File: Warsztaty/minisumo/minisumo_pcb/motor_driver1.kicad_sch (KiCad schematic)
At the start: 6 parts, among them U2 TB6612FNG

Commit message: stan przed usunięciem jednego czujnika lini
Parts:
- C3, C6: footprint Capacitor_SMD:C_0805_2012Metric_Pad1.18x1.45mm_HandSolder -> Capacitor_SMD:C_0805_2012Metric
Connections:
- net MOTOR_IN1: now reaches M1.2, U2.1 (AO1), U2.11 (BO1), U2.12 (BO1), U2.2 (AO1)
- net MOTOR_IN2: now reaches M1.1, U2.5 (AO2), U2.6 (AO2), U2.7 (BO2), U2.8 (BO2)
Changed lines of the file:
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@@
+		)
+	)
+	(label "MOTOR_IN1"
+		(at 76.2 45.72 0)
+		(fields_autoplaced yes)
+		(effects
+			(font
+				(size 1.27 1.27)
+			)
+			(justify left bottom)
+		)
+	)
+	(label "MOTOR_IN2"
+		(at 76.2 55.88 0)
+		(fields_autoplaced yes)
+		(effects
+			(font
+				(size 1.27 1.27)
+			)
+			(justify left bottom)
 		)
 	)
@@
 			)
 		)
-		(property "Footprint" "Capacitor_SMD:C_0805_2012Metric_Pad1.18x1.45mm_HandSolder"
+		(property "Footprint" "Capacitor_SMD:C_0805_2012Metric"
 			(at 31.75 30.48 0)
 			(effects
@@
 			)
 		)
-		(property "Footprint" "Capacitor_SMD:C_0805_2012Metric_Pad1.18x1.45mm_HandSolder"
+		(property "Footprint" "Capacitor_SMD:C_0805_2012Metric"
 			(at 72.39 29.21 0)
 			(effects

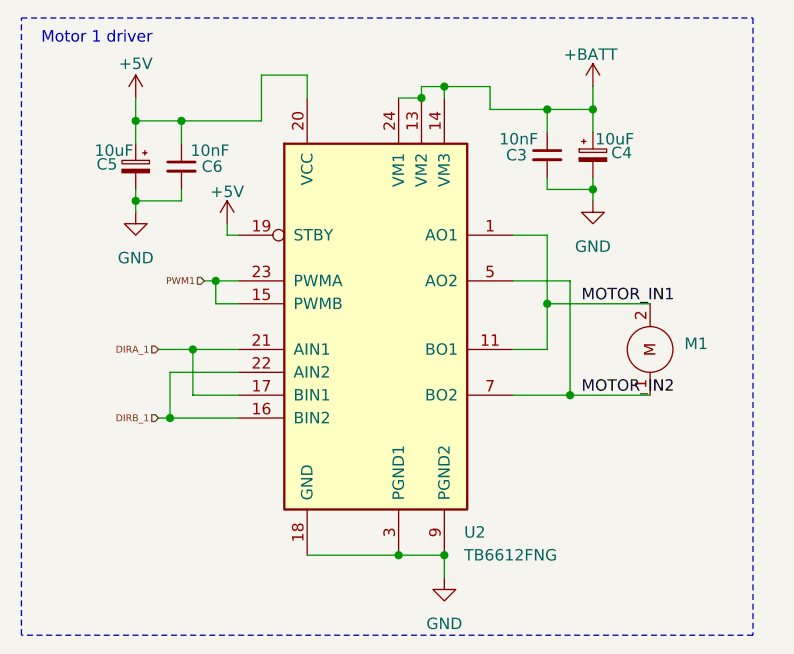
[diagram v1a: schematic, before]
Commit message: Wstępny wyglad robota i płytki
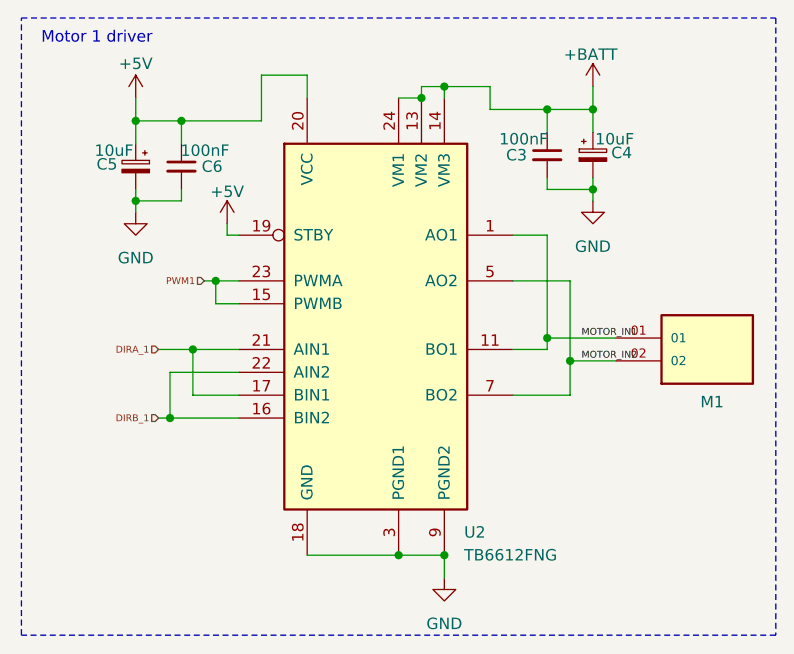
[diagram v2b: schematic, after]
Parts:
- removed M1: ~, Motors_KoNaR:KoNaR_Motor, symbol Motors_KoNaR:Motor
- added M1: HTSW-102-08-L-S, HTSW-102-08-L-S:SAMTEC_HTSW-102-08-L-S, symbol HTSW-102-08-L-S:HTSW-102-08-L-S
- C3, C6: value 10nF -> 100nF
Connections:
- net MOTOR_IN1: now also M1.01
- net MOTOR_IN2: now also M1.02
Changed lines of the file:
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@@
+	)
+	(junction
+		(at 74.93 52.07)
+		(diameter 0)
+		(color 0 0 0 0)
 	)
 	(junction
@@
 	)
 	(junction
-		(at 72.39 45.72)
+		(at 72.39 49.53)
 		(diameter 0)
 		(color 0 0 0 0)
@@
 	)
 	(junction
-		(at 74.93 55.88)
-		(diameter 0)
-		(color 0 0 0 0)
-	)
-	(junction
 		(at 30.48 58.42)
 		(diameter 0)
@@
 	(wire
 		(pts
-			(xy 72.39 38.1) (xy 72.39 45.72)
-		)
-		(stroke
-			(width 0)
-			(type default)
-		)
-	)
-	(wire
-		(pts
 			(xy 30.48 53.34) (xy 30.48 58.42)
 		)
@@
 	(wire
 		(pts
-			(xy 74.93 43.18) (xy 74.93 55.88)
+			(xy 74.93 43.18) (xy 74.93 52.07)
 		)
 		(stroke
@@
 	(wire
 		(pts
-			(xy 72.39 45.72) (xy 83.82 45.72)
-		)
-		(stroke
-			(width 0)
-			(type default)
-		)
-	)
-	(wire
-		(pts
 			(xy 45.72 73.66) (xy 55.88 73.66)
 		)
@@
 	(wire
 		(pts
+			(xy 72.39 49.53) (xy 80.01 49.53)
+		)
+		(stroke
+			(width 0)
+			(type default)
+		)
+	)
+	(wire
+		(pts
 			(xy 36.83 36.83) (xy 36.83 38.1)
 		)
@@
 	(wire
 		(pts
+			(xy 72.39 38.1) (xy 72.39 49.53)
+		)
+		(stroke
+			(width 0)
+			(type default)
+		)
+	)
+	(wire
+		(pts
+			(xy 74.93 52.07) (xy 80.01 52.07)
+		)
+		(stroke
+			(width 0)
+			(type default)
+		)
+	)
+	(wire
+		(pts
+			(xy 72.39 49.53) (xy 72.39 50.8)
+		)
+		(stroke
+			(width 0)
+			(type default)
+		)
+	)
+	(wire
+		(pts
+			(xy 74.93 52.07) (xy 74.93 55.88)
+		)
+		(stroke
+			(width 0)
+			(type default)
+		)
+	)
+	(wire
+		(pts
 			(xy 31.75 25.4) (xy 31.75 27.94)
 		)
@@
 	(wire
 		(pts
-			(xy 72.39 45.72) (xy 72.39 50.8)
-		)
-		(stroke
-			(width 0)
-			(type default)
-		)
-	)
-	(wire
-		(pts
 			(xy 45.72 20.32) (xy 45.72 22.86)
 		)
@@
 		(pts
 			(xy 60.96 21.59) (xy 66.04 21.59)
-		)
-		(stroke
-			(width 0)
-			(type default)
-		)
-	)
-	(wire
-		(pts
-			(xy 74.93 55.88) (xy 83.82 55.88)
 		)
 		(stroke
@@
 	(rectangle
 		(start 13.97 13.97)
-		(end 95.25 82.55)
+		(end 97.79 82.55)
 		(stroke
 			(width 0)
@@
 	)
 	(label "MOTOR_IN1"
-		(at 76.2 45.72 0)
+		(at 76.2 49.53 0)
 		(fields_autoplaced yes)
 		(effects
 			(font
-				(size 1.27 1.27)
+				(size 0.762 0.762)
 			)
 			(justify left bottom)
@@
 	)
 	(label "MOTOR_IN2"
-		(at 76.2 55.88 0)
+		(at 76.2 52.07 0)
 		(fields_autoplaced yes)
 		(effects
 			(font
-				(size 1.27 1.27)
+				(size 0.762 0.762)
 			)
 			(justify left bottom)
@@
 	)
 	(symbol
+		(lib_id "HTSW-102-08-L-S:HTSW-102-08-L-S")
+		(at 90.17 49.53 0)
+		(unit 1)
+		(exclude_from_sim no)
+		(in_bom yes)
+		(on_board yes)
+		(dnp no)
+		(property "Reference" "M1"
+			(at 89.408 56.642 0)
+			(effects
+				(font
+					(size 1.27 1.27)
+				)
+				(justify left)
+			)
+		)
+		(property "Value" "HTSW-102-08-L-S"
+			(at 76.962 44.704 0)
+			(effects
+				(font
+					(size 1.27 1.27)
+				)
+				(justify left)
+				(hide yes)
+			)
+		)
+		(property "Footprint" "HTSW-102-08-L-S:SAMTEC_HTSW-102-08-L-S"
+			(at 90.17 49.53 0)
+			(effects
+				(font
+					(size 1.27 1.27)
+				)
+				(justify bottom)
+				(hide yes)
+			)
+		)
+		(property "Datasheet" ""
+			(at 90.17 49.53 0)
+			(effects
+				(font
+					(size 1.27 1.27)
+				)
+				(hide yes)
+			)
+		)
+		(property "Description" ""
+			(at 90.17 49.53 0)
+			(effects
+				(font
+					(size 1.27 1.27)
+				)
+				(hide yes)
+			)
+		)
+		(property "MF" "Samtec Inc."
+			(at 90.17 49.53 0)
+			(effects
+				(font
+					(size 1.27 1.27)
+				)
+				(justify bottom)
+				(hide yes)
+			)
+		)
+		(property "Description_1" "\nConn Unshrouded Header HDR 2 POS 2.54mm Solder ST Top Entry Thru-Hole Bag\n"
+			(at 90.17 49.53 0)
+			(effects
+				(font
+					(size 1.27 1.27)
+				)
+				(justify bottom)
+				(hide yes)
+			)
+		)
+		(property "Package" "None"
+			(at 90.17 49.53 0)
+			(effects
+				(font
+					(size 1.27 1.27)
+				)
+				(justify bottom)
+				(hide yes)
+			)
+		)
+		(property "Price" "None"
+			(at 90.17 49.53 0)
+			(effects
+				(font
+					(size 1.27 1.27)
+				)
+				(justify bottom)
+				(hide yes)
+			)
+		)
+		(property "Check_prices" "https://www.snapeda.com/parts/HTSW-102-08-L-S/Samtec/view-part/?ref=eda"
+			(at 90.17 49.53 0)
+			(effects
+				(font
+					(size 1.27 1.27)
+				)
+				(justify bottom)
+				(hide yes)
+			)
+		)
+		(property "SnapEDA_Link" "https://www.snapeda.com/parts/HTSW-102-08-L-S/Samtec/view-part/?ref=snap"
+			(at 90.17 49.53 0)
+			(effects
+				(font
+					(size 1.27 1.27)
+				)
+				(justify bottom)
+				(hide yes)
+			)
+		)
+		(property "MP" "HTSW-102-08-L-S"
+			(at 90.17 49.53 0)
+			(effects
+				(font
+					(size 1.27 1.27)
+				)
+				(justify bottom)
+				(hide yes)
+			)
+		)
+		(property "Availability" "In Stock"
+			(at 90.17 49.53 0)
+			(effects
+				(font
+					(size 1.27 1.27)
+				)
+				(justify bottom)
+				(hide yes)
+			)
+		)
+		(property "Purchase-URL" "https://pricing.snapeda.com/search/part/HTSW-102-25-G-S/?ref=eda"
+			(at 90.17 49.53 0)
+			(effects
+				(font
+					(size 1.27 1.27)
+				)
+				(justify bottom)
+				(hide yes)
+			)
+		)
+		(pin "02"
+		)
+		(pin "01"
+		)
+		(instances
+			(project "minisumo_pcb"
+				(path "/7b99a4ad-c15f-48f5-acdf-b2b295c8ee3b/6ae141c6-db4a-4bb1-a0f3-35ba0e4d6945"
+					(reference "M1")
+					(unit 1)
+				)
+			)
+		)
+	)
+	(symbol
 		(lib_id "Device:C_Small")
 		(at 31.75 30.48 0)
@@
 			)
 		)
-		(property "Value" "10nF"
+		(property "Value" "100nF"
 			(at 37.084 28.702 0)
 			(effects
@@
 				(path "/7b99a4ad-c15f-48f5-acdf-b2b295c8ee3b/6ae141c6-db4a-4bb1-a0f3-35ba0e4d6945"
 					(reference "C5")
-					(unit 1)
-				)
-			)
-		)
-	)
-	(symbol
-		(lib_id "Motors_KoNaR:Motor")
-		(at 83.82 50.8 90)
-		(unit 1)
-		(exclude_from_sim no)
-		(in_bom yes)
-		(on_board yes)
-		(dnp no)
-		(fields_autoplaced yes)
-		(property "Reference" "M1"
-			(at 87.63 50.1649 90)
-			(effects
-				(font
-					(size 1.27 1.27)
-				)
-				(justify right)
-			)
-		)
-		(property "Value" "~"
-			(at 87.63 52.07 90)
-			(effects
-				(font
-					(size 1.27 1.27)
-				)
-				(justify right)
-			)
-		)
-		(property "Footprint" "Motors_KoNaR:KoNaR_Motor"
-			(at 87.884 50.8 0)
-			(effects
-				(font
-					(size 1.27 1.27)
-				)
-				(hide yes)
-			)
-		)
-		(property "Datasheet" ""
-			(at 83.82 50.8 0)
-			(effects
-				(font
-					(size 1.27 1.27)
-				)
-				(hide yes)
-			)
-		)
-		(property "Description" ""
-			(at 83.82 50.8 0)
-			(effects
-				(font
-					(size 1.27 1.27)
-				)
-				(hide yes)
-			)
-		)
-		(pin "1"
-		)
-		(pin "2"
-		)
-		(instances
-			(project "minisumo_pcb"
-				(path "/7b99a4ad-c15f-48f5-acdf-b2b295c8ee3b/6ae141c6-db4a-4bb1-a0f3-35ba0e4d6945"
-					(reference "M1")
 					(unit 1)
 				)
@@
 			)
 		)
-		(property "Value" "10nF"
+		(property "Value" "100nF"
 			(at 67.056 27.432 0)
 			(effects

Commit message: koncowy projekt plytki i chyba model tez
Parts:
- renumbered U2 to M_DRIVER1
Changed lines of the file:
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@@
 		(dnp no)
 		(fields_autoplaced yes)
-		(property "Reference" "U2"
+		(property "Reference" "M_DRIVER1"
 			(at 63.1541 71.12 0)
 			(effects
@@
 			(project "minisumo_pcb"
 				(path "/7b99a4ad-c15f-48f5-acdf-b2b295c8ee3b/6ae141c6-db4a-4bb1-a0f3-35ba0e4d6945"
-					(reference "U2")
+					(reference "M_DRIVER1")
 					(unit 1)
 				)
